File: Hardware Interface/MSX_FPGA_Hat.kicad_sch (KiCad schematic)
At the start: 31 parts, among them J1 J1, J2 J2, J5 Conn_01x03_Female, U1 74LVC245A, U2 74LVC245A, U3 74LVC245A, U4 74LVC245A, U5 74LVC245A, U6 LM1117-3.3

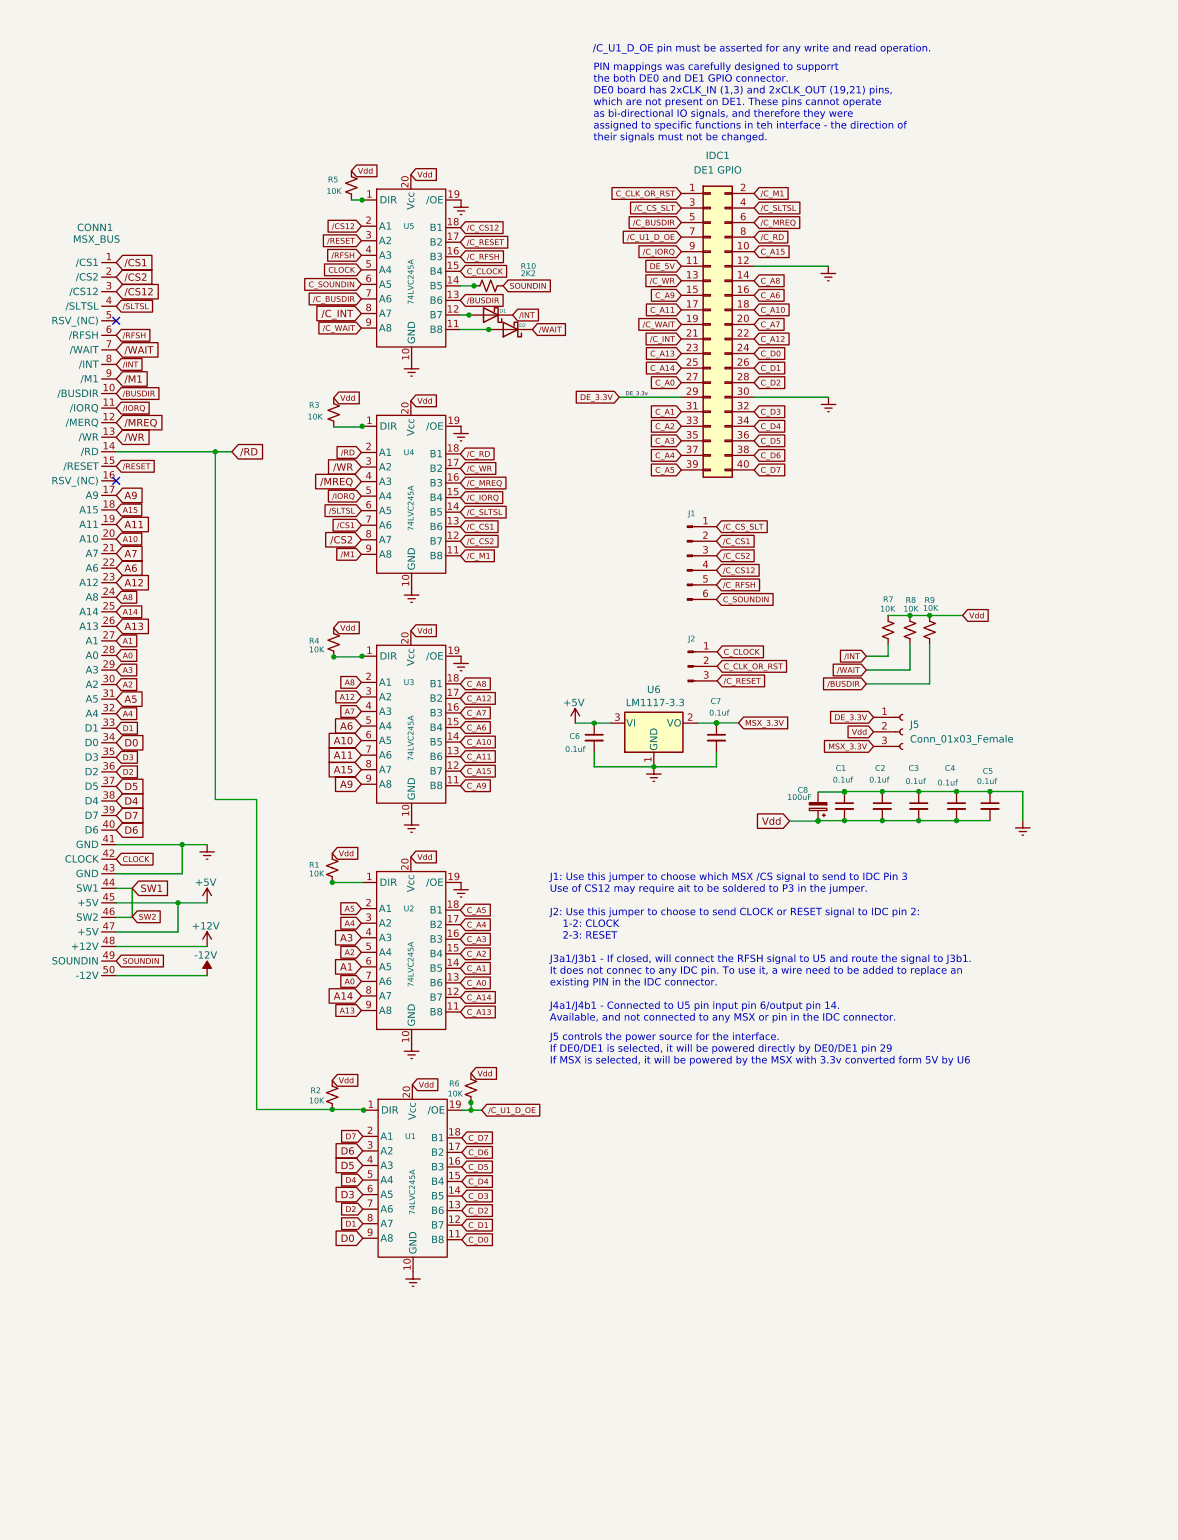
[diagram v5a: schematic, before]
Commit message: Added pull-up with 4 x resistor arrays; added reset button
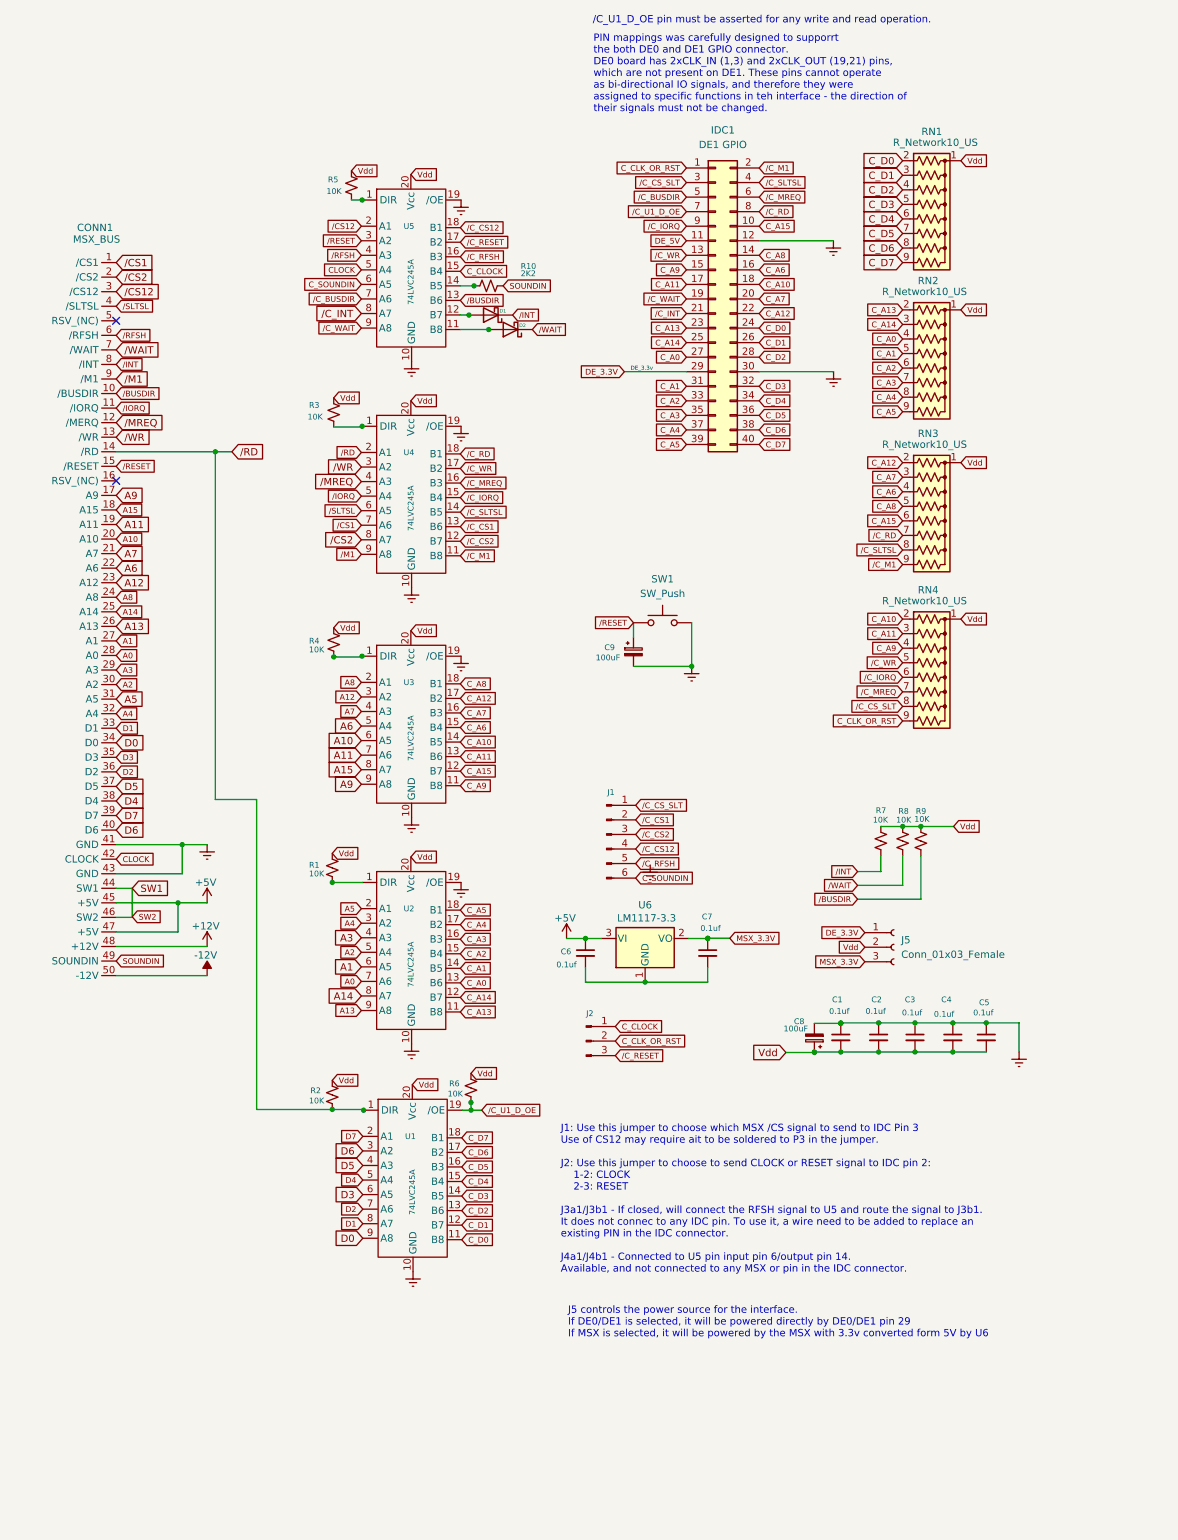
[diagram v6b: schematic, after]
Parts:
- added C9: 100uF, Capacitor_THT:CP_Radial_D6.3mm_P2.50mm, symbol Device:C_Polarized_Small
- added RN1, RN2, RN3, RN4: R_Network10_US, Resistor_THT:R_Array_SIP9, symbol Device:R_Network08_US
- added SW1: SW_Push, Connector_PinSocket_2.54mm:PinSocket_1x02_P2.54mm_Vertical, symbol Switch:SW_Push
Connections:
- net C_A0: now also RN2.4 (R3)
- net C_A1: now also RN2.5 (R4)
- net C_A10: now also RN4.2 (R1)
- net C_A11: now also RN4.3 (R2)
- net C_A12: now also RN3.2 (R1)
- net C_A13: now also RN2.2 (R1)
- net C_A14: now also RN2.3 (R2)
- net C_A15: now also RN3.6 (R5)
- net C_A2: now also RN2.6 (R5)
- net C_A3: now also RN2.7 (R6)
- net C_A4: now also RN2.8 (R7)
- net C_A5: now also RN2.9 (R8)
- net C_A6: now also RN3.4 (R3)
- net C_A7: now also RN3.3 (R2)
- net C_A8: now also RN3.5 (R4)
- net C_A9: now also RN4.4 (R3)
- net C_CLK_OR_RST: now also RN4.9 (R8)
- net C_D0: now also RN1.2 (R1)
- net C_D1: now also RN1.3 (R2)
- net C_D2: now also RN1.4 (R3)
- net C_D3: now also RN1.5 (R4)
- net C_D4: now also RN1.6 (R5)
- net C_D5: now also RN1.7 (R6)
- net C_D6: now also RN1.8 (R7)
- net C_D7: now also RN1.9 (R8)
- net GNDREF: now also C9.2, SW1.2; no longer C6.2, C7.2, U6.1 (GND)
- net Vdd: now also RN1.1 (common), RN2.1 (common), RN3.1 (common), RN4.1 (common)
- net /C_CS_SLT: now also RN4.8 (R7)
- net /C_IORQ: now also RN4.6 (R5)
- net /C_M1: now also RN3.9 (R8)
- net /C_MREQ: now also RN4.7 (R6)
- net /C_RD: now also RN3.7 (R6)
- net /C_SLTSL: now also RN3.8 (R7)
- net /C_WR: now also RN4.5 (R4)
- net /RESET: now also C9.1, SW1.1
- new net: C6.2, C7.2, U6.1 (GND)
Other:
- moved on the sheet: C1, C2, C3, C4, C5, C6, C7, C8, IDC1, J1, J2, J5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

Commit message: V 1.5
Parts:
- added RN5: 10K, Resistor_THT:R_Array_SIP9, symbol Device:R_Network08_US
- RN1, RN2, RN3, RN4: value R_Network10_US -> 10K
- U1, U2, U3, U4, U5: value 74LVC245A -> 74LS641-1DW
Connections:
- net +5V: now also R7.1, R8.1, R9.1, RN5.1 (common)
- net D0: now also RN5.2 (R1)
- net D1: now also RN5.3 (R2)
- net D2: now also RN5.4 (R3)
- net D3: now also RN5.5 (R4)
- net D4: now also RN5.6 (R5)
- net D5: now also RN5.7 (R6)
- net D6: now also RN5.8 (R7)
- net D7: now also RN5.9 (R8)
- net GNDREF: now also C6.2, C7.2, U6.1 (GND)
- net Vdd: no longer R7.1, R8.1, R9.1
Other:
- moved on the sheet: C6, C7, C9, J1, J2, R7, R8, R9, SW1, U6

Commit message: v1.6
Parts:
- removed D1, D2: BAT43, Resistor_THT:R_Axial_DIN0207_L6.3mm_D2.5mm_P7.62mm_Horizontal, symbol Device:D_Schottky
- removed R1, R3, R4, R5: 10K, Resistor_THT:R_Axial_DIN0207_L6.3mm_D2.5mm_P7.62mm_Horizontal, symbol Device:R_Small_US
- removed R10: 2K2, Resistor_THT:R_Axial_DIN0207_L6.3mm_D2.5mm_P7.62mm_Horizontal, symbol Device:R_Small_US
- added D1: 1N5817, Diode_THT:D_DO-41_SOD81_P10.16mm_Horizontal, symbol Diode:1N5817
- added Q1, Q2: 2N3904, Package_TO_SOT_THT:TO-92_Inline, symbol Transistor_BJT:2N3904
- added R12, R13: 2K2, Resistor_THT:R_Axial_DIN0207_L6.3mm_D2.5mm_P7.62mm_Horizontal, symbol Device:R_Small_US
- C8: value 100uF -> 10uF
- J1: footprint Connector_PinHeader_2.54mm:PinHeader_2x03_P2.54mm_Vertical -> Connector_PinHeader_2.54mm:PinHeader_1x03_P2.54mm_Vertical; symbol Connector:Conn_01x06_Male -> Connector:Conn_01x03_Pin
- R7, R8: value 10K -> 4K7
- U1, U2, U3, U4, U5: value 74LS641-1DW -> 74LVC245
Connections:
- net C_CLK_OR_RST: no longer IDC1.1 (Pin_1)
- net GNDREF: now also C1.2, C2.2, C3.2, C4.2, C5.2, Q1.1 (E), Q2.1 (E); no longer C1.1, C2.1, C3.1, C4.1, C5.1
- net Vdd: now also C1.1, C2.1, C3.1, C4.1, C5.1, R7.1, R8.1, U2.1 (DIR), U3.1 (DIR), U4.1 (DIR), U4.7 (A6), U4.8 (A7), U5.1 (DIR), U5.2 (A1), U5.4 (A3), U5.6 (A5); no longer C1.2, C2.2, C3.2, C4.2, C5.2, C8.1
- net /C_CS1: no longer J1.2 (Pin_2)
- net /C_CS2: no longer J1.3 (Pin_3)
- net /C_CS_SLT: no longer IDC1.3 (Pin_3), J1.1 (Pin_1)
- net /C_INT: now also R7.2, U5.9 (A8); no longer U5.8 (A7)
- net /C_M1: now also IDC1.3 (Pin_3); no longer IDC1.2 (Pin_2)
- net /C_WAIT: now also R8.2, U5.8 (A7); no longer U5.9 (A8)
- net /INT: now also Q2.3 (C); no longer R7.2
- net /RD: now also J1.3 (Pin_3); no longer R2.2, U1.1 (DIR)
- net /WAIT: now also Q1.3 (C); no longer R8.2
- net at U5.11 (B8): now also R13.2
- net at U5.12 (B7): now also R12.2
- net +5V renamed Vcc
- net Vcc: now also C8.1, D1.1 (K); no longer CONN1.45 (+5V), CONN1.47 (+5V), R7.1, R8.1
- removed net C_SOUNDIN: J1.6 (Pin_6), U5.6 (A5)
- net SOUNDIN: no longer names the net of CONN1.49 (SOUNDIN)
- net /CS1: no longer names the net of CONN1.1 (/CS1)
- net /CS1: no longer U4.7 (A6)
- net /CS12: no longer names the net of CONN1.3 (/CS12)
- net /CS12: no longer U5.2 (A1)
- net /CS2: no longer names the net of CONN1.2 (/CS2)
- net /CS2: no longer U4.8 (A7)
- net /C_CS12: no longer names the net of U5.18 (B1)
- net /C_CS12: no longer J1.4 (Pin_4)
- net /C_RFSH: no longer names the net of U5.16 (B3)
- net /C_RFSH: no longer J1.5 (Pin_5)
- net /RFSH: no longer names the net of CONN1.6 (/RFSH)
- net /RFSH: no longer U5.4 (A3)
- new net: Q2.2 (B), R13.1
- new net: Q1.2 (B), R12.1
- new net: CONN1.45 (+5V), CONN1.47 (+5V), D1.2 (A)
- new net C_DATA_DIR: IDC1.2 (Pin_2), J1.1 (Pin_1)
- new net C_RST: IDC1.1 (Pin_1)
- new net /U1_D_DIR: J1.2 (Pin_2), R2.2, U1.1 (DIR)
- no-connect marks 2 -> 10
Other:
- company: RCC -> RCC6
- moved on the sheet: C1, C2, C3, C4, C5, C6, C7, C8, C9, IDC1, J2, J5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
